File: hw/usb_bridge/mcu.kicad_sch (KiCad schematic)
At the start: 10 parts, among them J3 SWD, J4 BOOT, U7 STM32G0B1CBT, Y2 HCI XC53G2-8.000-F12NJHP

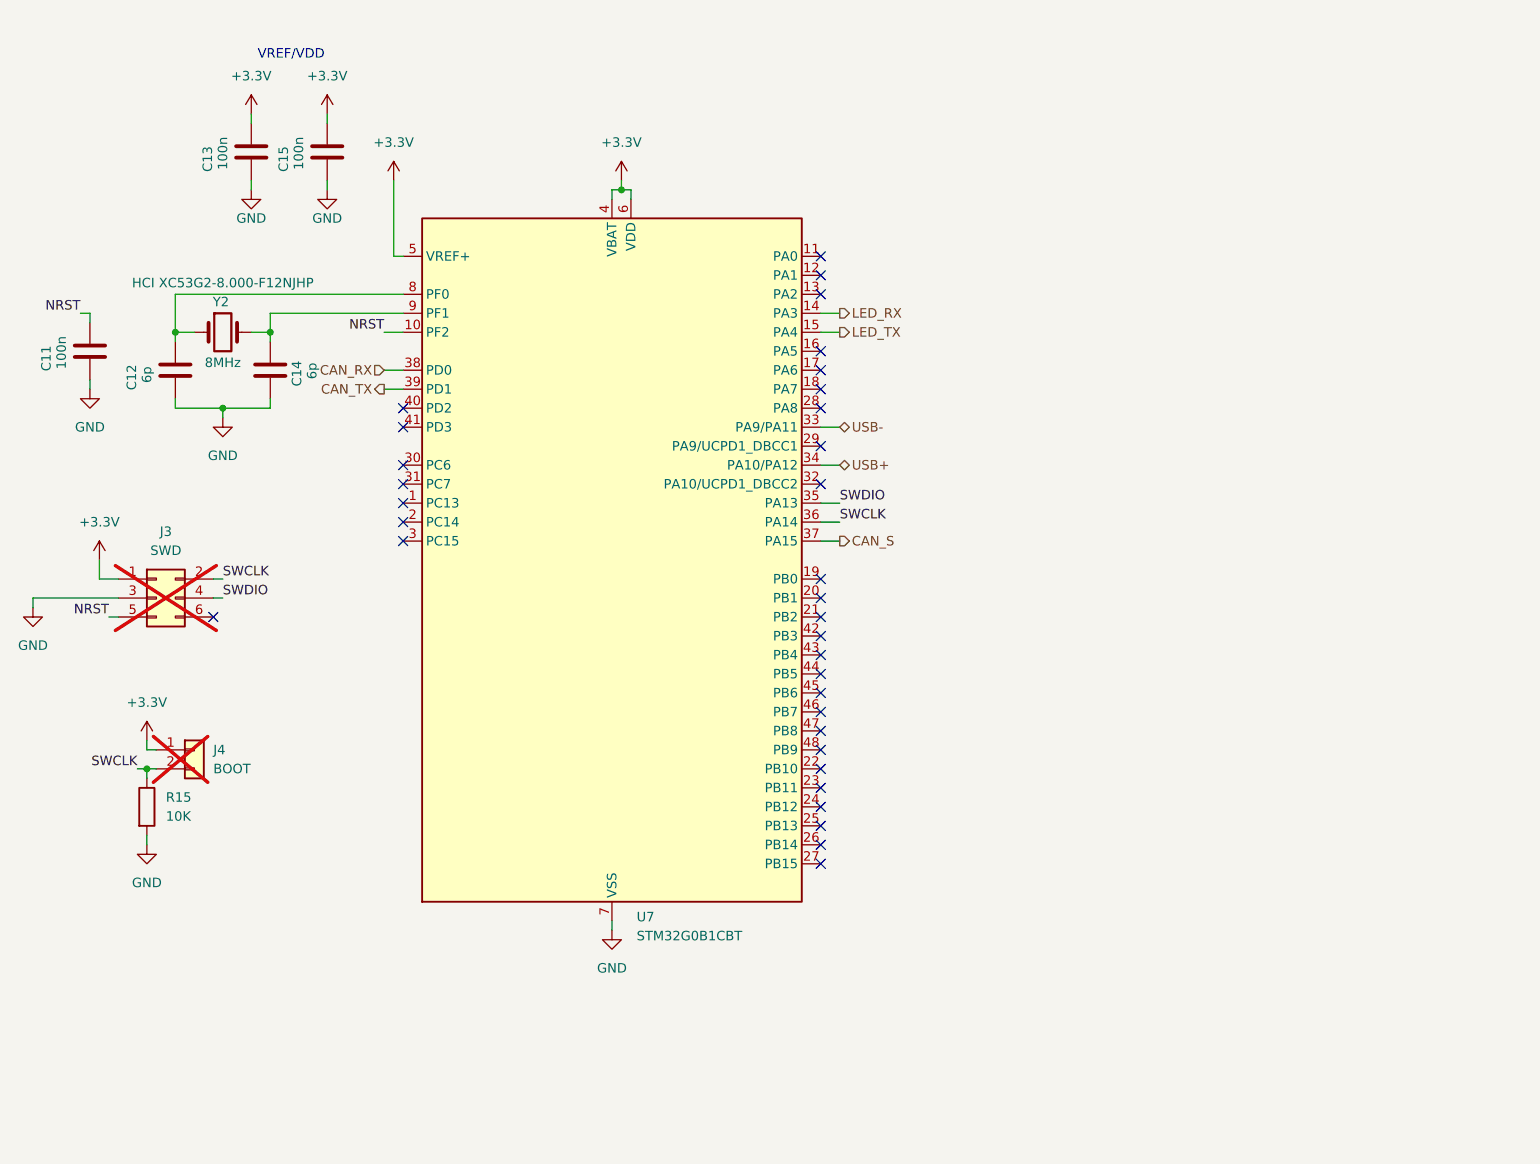
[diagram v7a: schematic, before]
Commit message: usb_bridge: Major LED fixes, replace USB-C protection circuit, add RS485 pullups, add mounting holes
Signed-off-by: Mateusz Pajak <22417805+Tai-Min@users.noreply.github.com>
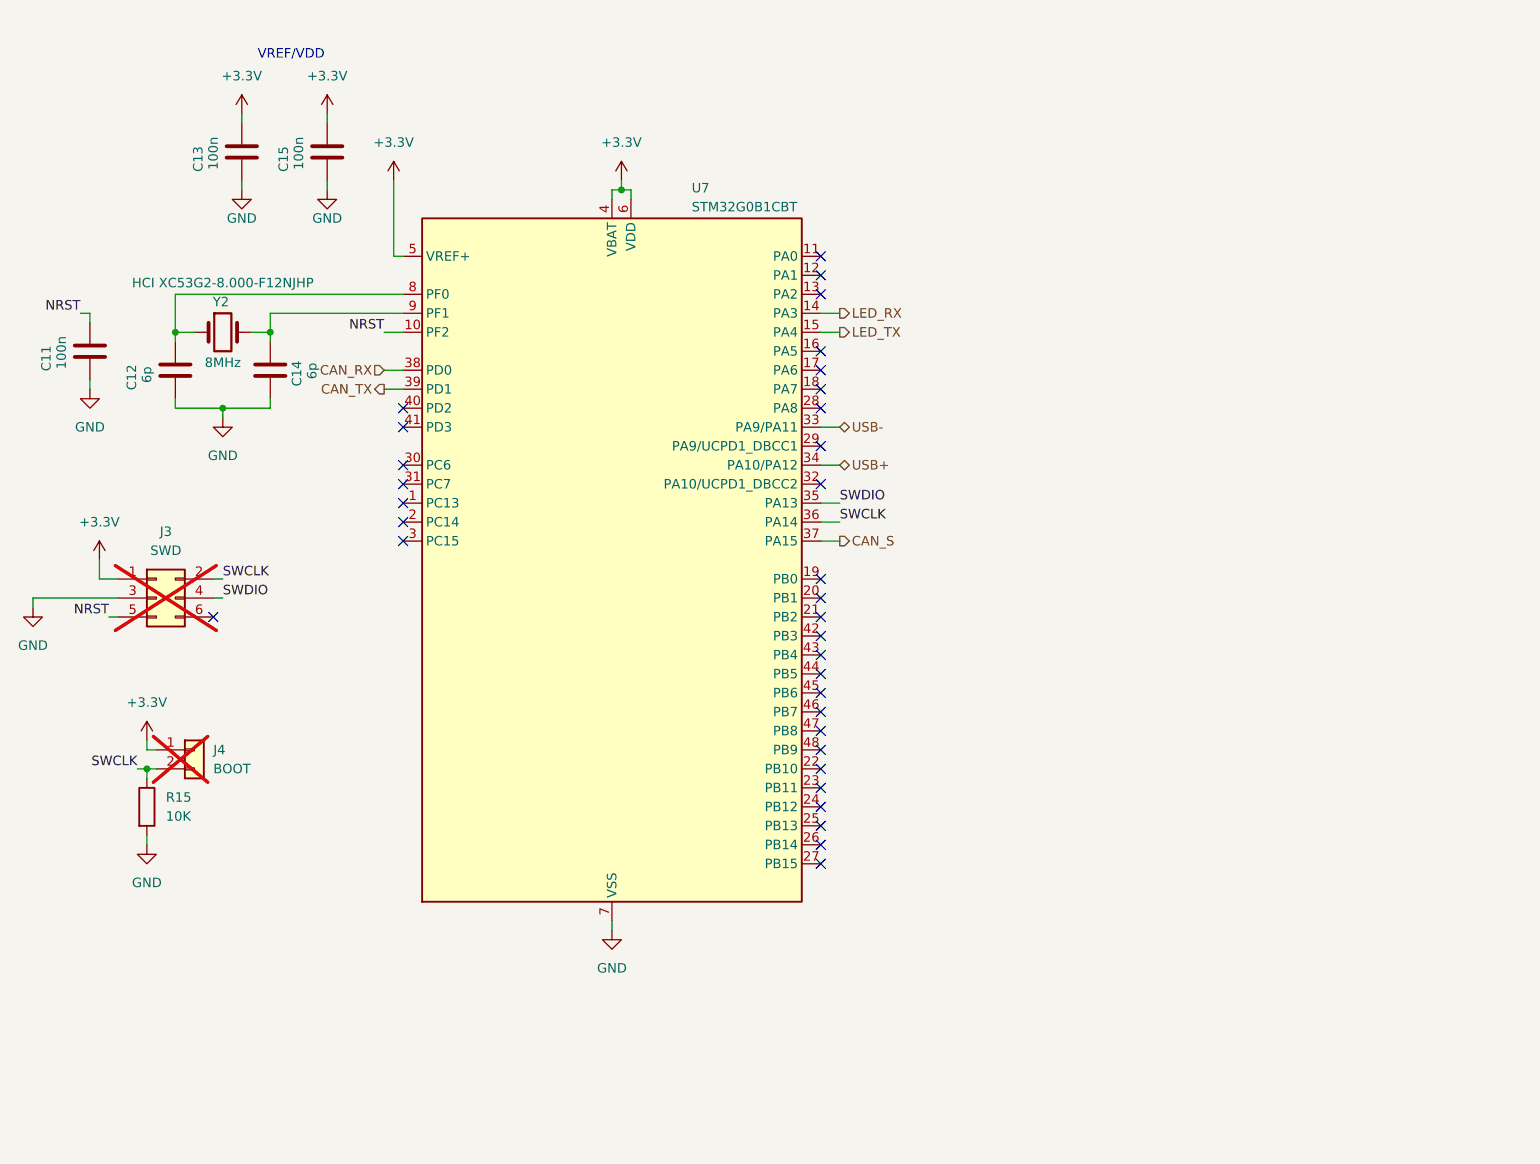
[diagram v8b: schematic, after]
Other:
- moved on the sheet: C13
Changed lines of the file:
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@@
 	(wire
 		(pts
-			(xy 113.03 41.91) (xy 113.03 43.18)
+			(xy 111.76 41.91) (xy 111.76 43.18)
 		)
 		(stroke
@@
 	(wire
 		(pts
-			(xy 113.03 50.8) (xy 113.03 52.07)
+			(xy 111.76 50.8) (xy 111.76 52.07)
 		)
 		(stroke
@@
 	(symbol
 		(lib_id "power:GND")
-		(at 113.03 52.07 0)
+		(at 111.76 52.07 0)
 		(unit 1)
 		(exclude_from_sim no)
@@
 		(dnp no)
 		(property "Reference" "#PWR047"
-			(at 113.03 58.42 0)
+			(at 111.76 58.42 0)
 			(effects
 				(font
@@
 		)
 		(property "Value" "GND"
-			(at 113.03 55.88 0)
+			(at 111.76 55.88 0)
 			(effects
 				(font
@@
 		)
 		(property "Footprint" ""
-			(at 113.03 52.07 0)
+			(at 111.76 52.07 0)
 			(effects
 				(font
@@
 		)
 		(property "Datasheet" ""
-			(at 113.03 52.07 0)
+			(at 111.76 52.07 0)
 			(effects
 				(font
@@
 		)
 		(property "Description" "Power symbol creates a global label with name \"GND\" , ground"
-			(at 113.03 52.07 0)
+			(at 111.76 52.07 0)
 			(effects
 				(font
@@
 		(dnp no)
 		(property "Reference" "U7"
-			(at 164.592 149.352 0)
+			(at 171.958 51.816 0)
 			(effects
 				(font
@@
 		)
 		(property "Value" "STM32G0B1CBT"
-			(at 164.592 151.892 0)
+			(at 171.958 54.356 0)
 			(effects
 				(font
@@
 	(symbol
 		(lib_id "power:+3.3V")
-		(at 113.03 41.91 0)
+		(at 111.76 41.91 0)
 		(unit 1)
 		(exclude_from_sim no)
@@
 		(fields_autoplaced yes)
 		(property "Reference" "#PWR046"
-			(at 113.03 45.72 0)
+			(at 111.76 45.72 0)
 			(effects
 				(font
@@
 		)
 		(property "Value" "+3.3V"
-			(at 113.03 36.83 0)
+			(at 111.76 36.83 0)
 			(effects
 				(font
@@
 		)
 		(property "Footprint" ""
-			(at 113.03 41.91 0)
+			(at 111.76 41.91 0)
 			(effects
 				(font
@@
 		)
 		(property "Datasheet" ""
-			(at 113.03 41.91 0)
+			(at 111.76 41.91 0)
 			(effects
 				(font
@@
 		)
 		(property "Description" "Power symbol creates a global label with name \"+3.3V\""
-			(at 113.03 41.91 0)
+			(at 111.76 41.91 0)
 			(effects
 				(font
@@
 	(symbol
 		(lib_id "Device:C")
-		(at 113.03 46.99 180)
+		(at 111.76 46.99 180)
 		(unit 1)
 		(exclude_from_sim no)
@@
 		(dnp no)
 		(property "Reference" "C13"
-			(at 107.188 46.228 90)
+			(at 105.918 46.228 90)
 			(effects
 				(font
@@
 		)
 		(property "Value" "100n"
-			(at 109.22 44.9581 90)
+			(at 107.95 44.9581 90)
 			(effects
 				(font
@@
 		)
 		(property "Footprint" "Capacitor_SMD:C_0603_1608Metric"
-			(at 112.0648 43.18 0)
+			(at 110.7948 43.18 0)
 			(effects
 				(font
@@
 		)
 		(property "Datasheet" "~"
-			(at 113.03 46.99 0)
+			(at 111.76 46.99 0)
 			(effects
 				(font
@@
 		)
 		(property "Description" "Unpolarized capacitor"
-			(at 113.03 46.99 0)
+			(at 111.76 46.99 0)
 			(effects
 				(font
@@
 		)
 		(property "LCSC Part #" "C66501"
-			(at 113.03 46.99 90)
-			(effects
-				(font
+			(at 111.76 46.99 90)
+			(effects
+				(font
